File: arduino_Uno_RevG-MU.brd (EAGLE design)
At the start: 107 x 76.2 mm, 48 parts, among them IC3 ADC, U4 ARDUINOR3-DIMENSION

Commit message: updated
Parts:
- removed U$33: CS, LS_ELECTRIC:1X2_HEADER
- added U$14, U$15, U$16, U$17, U$20: 1X2_HEADER1X2, LS_ELECTRIC:1X2_HEADER
- moved U$9 10.1 mm to (86.0, 7.60), turned to 90 degrees
- moved R14 10.1 mm to (88.2, 7.68), turned to 270 degrees
- moved R5 7.53 mm to (88.2, 25.7), turned to 270 degrees
- moved U$3 7.52 mm to (86.0, 25.7), turned to 90 degrees
- moved R15 6.59 mm to (88.2, 66.2), turned to 90 degrees
- moved U$12 6.54 mm to (86.1, 66.2), turned to 90 degrees
- moved U$10 6.31 mm to (90.7, 9.62), turned to 90 degrees
- moved U$36 5.25 mm to (93.9, 65.6)
- moved U$6 4.46 mm to (86.1, 44.0), turned to 90 degrees
- moved R7 4.43 mm to (88.2, 44.0), turned to 270 degrees
- moved R6 3.91 mm to (88.1, 48.1), turned to 90 degrees
- moved U$4 3.86 mm to (86.1, 48.0), turned to 90 degrees
- moved U$34 3.76 mm to (93.9, 10.9)
- moved U$11 3.62 mm to (90.7, 27.6), turned to 90 degrees
- moved U$19 2.76 mm to (90.6, 64.3), turned to 90 degrees
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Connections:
- removed net IO6: U4.D6
- new net N$4: U$20.2, U$40.4
- new net N$5: U$20.1, U$40.5
- new net SS0: U$14.1, U4.D10
- new net SS1: U$15.1, U4.D8
- new net SS2: U$16.1, U4.D7
- new net SS3: U$17.1, U4.D6
- net CS3: no longer U$33.1
- net CS4: no longer U$33.2
- net IO4: now also U$40.2; no longer U$40.4
- net IO5: now also U$40.1; no longer U$40.5
- net N$11: now also U$1.GND_INV
- net N$15: now also U$36.GND_INV
- net N$23: now also U$34.GND_INV
- net N$34: now also U$35.GND_INV
- net RX: no longer U$40.1
- net SS: now also U$14.2, U$15.2, U$16.2, U$17.2; no longer U4.D10
- net TX: no longer U$40.2
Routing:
- net TX: track 60.7 -> 0.00 mm
- net RX: track 60.4 -> 0.00 mm
- net SS: track 12.0 -> 41.1 mm, vias 0 -> 2
- net IO5: track 65.9 -> 45.6 mm
- net 5VDC_COM_I: track 134.0 -> 149.2 mm, vias 12 -> 5
- net N$15: track 5.91 -> 16.3 mm
- net N$23: track 5.92 -> 16.2 mm
- net N$11: track 5.92 -> 16.2 mm
- net N$34: track 5.98 -> 16.0 mm
- net IO4: track 65.0 -> 55.5 mm, vias 1 -> 3
- net SS3: track 0.00 -> 8.86 mm
- net SS0: track 0.00 -> 8.11 mm
- net SS2: track 0.00 -> 8.05 mm
- net SS1: track 0.00 -> 7.99 mm
- net CS3: track 7.75 -> 0.00 mm
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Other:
- board text added: "DI_4"
- board text added: "DI_5"
- board text added: "INT1"

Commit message: First board order
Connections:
- net 24GND renamed P_GND
- net 24VDC renamed PWR
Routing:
- net PWR: track 7.48 -> 6.94 mm
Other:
- board text added: "5V+"
- board text added: "GND"
- board text added: "PROX"
- board text added: "PWR"
- board text added: "P_GND"
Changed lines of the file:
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@@
 <text x="13.6" y="55.6" size="1.27" layer="21">DI_4</text>
 <text x="13.4" y="58.4" size="1.27" layer="21">DI_5</text>
+<text x="13.6" y="15.5" size="1.016" layer="21">PWR</text>
+<text x="13" y="17.9" size="1.016" layer="21">PROX</text>
+<text x="12.9" y="26.5" size="1.016" layer="21">P_GND</text>
+<text x="12.7" y="31" size="1.016" layer="21">GND</text>
+<text x="12.8" y="36.2" size="1.016" layer="21">5V+</text>
 </plain>
 <attributes>
@@
 <wire x1="16.285" y1="22.4" x2="16.245" y2="22.44" width="0.254" layer="1"/>
 </signal>
-<signal name="24GND">
-<contactref element="OP1" pad="3_CAT"/>
-<contactref element="C22" pad="2"/>
-<wire x1="14.3" y1="26.1" x2="14.3" y2="24.63" width="0.254" layer="1"/>
-<wire x1="14.355" y1="24.575" x2="14.3" y2="24.63" width="0.254" layer="1"/>
-<wire x1="18.39" y1="23.86" x2="19.86" y2="23.86" width="0.254" layer="1"/>
-<wire x1="19.86" y1="23.86" x2="19.9" y2="23.9" width="0.254" layer="1"/>
-<via x="19.9" y="23.9" extent="1-16" drill="0.35"/>
-<wire x1="19.9" y1="23.9" x2="18.3" y2="23.9" width="0.254" layer="16"/>
-<wire x1="18.3" y1="23.9" x2="16.1" y2="26.1" width="0.254" layer="16"/>
-<wire x1="16.1" y1="26.1" x2="15.1" y2="26.1" width="0.254" layer="16"/>
-<via x="15.1" y="26.1" extent="1-16" drill="0.35"/>
-<wire x1="15.1" y1="26.1" x2="14.3" y2="26.1" width="0.254" layer="1"/>
-<contactref element="U$40" pad="8"/>
-<wire x1="10.175" y1="25.18" x2="10.78" y2="24.575" width="0.254" layer="1"/>
-<wire x1="10.78" y1="24.575" x2="14.355" y2="24.575" width="0.254" layer="1"/>
-</signal>
-<signal name="24VDC">
-<contactref element="R13" pad="1"/>
-<contactref element="U$40" pad="10"/>
-<wire x1="10.175" y1="15.1" x2="11.1" y2="15.1" width="0.254" layer="1"/>
-<wire x1="11.1" y1="15.1" x2="13.5" y2="17.5" width="0.254" layer="1"/>
-<wire x1="13.5" y1="17.5" x2="13.5" y2="19.465" width="0.254" layer="1"/>
-<wire x1="13.5" y1="19.465" x2="14.345" y2="20.31" width="0.254" layer="1"/>
-</signal>
 <signal name="PROX">
 <contactref element="R16" pad="1"/>
@@
 <wire x1="13.79" y1="40.42" x2="10.175" y2="40.42" width="0.254" layer="1"/>
 </signal>
+<signal name="PWR">
+<contactref element="R13" pad="1"/>
+<contactref element="U$40" pad="10"/>
+<wire x1="10.175" y1="15.1" x2="14.345" y2="19.27" width="0.254" layer="1"/>
+<wire x1="14.345" y1="19.27" x2="14.345" y2="20.31" width="0.254" layer="1"/>
+</signal>
+<signal name="P_GND">
+<contactref element="OP1" pad="3_CAT"/>
+<contactref element="C22" pad="2"/>
+<wire x1="14.3" y1="26.1" x2="14.3" y2="24.63" width="0.254" layer="1"/>
+<wire x1="14.355" y1="24.575" x2="14.3" y2="24.63" width="0.254" layer="1"/>
+<wire x1="18.39" y1="23.86" x2="19.86" y2="23.86" width="0.254" layer="1"/>
+<wire x1="19.86" y1="23.86" x2="19.9" y2="23.9" width="0.254" layer="1"/>
+<via x="19.9" y="23.9" extent="1-16" drill="0.35"/>
+<wire x1="19.9" y1="23.9" x2="18.3" y2="23.9" width="0.254" layer="16"/>
+<wire x1="18.3" y1="23.9" x2="16.1" y2="26.1" width="0.254" layer="16"/>
+<wire x1="16.1" y1="26.1" x2="15.1" y2="26.1" width="0.254" layer="16"/>
+<via x="15.1" y="26.1" extent="1-16" drill="0.35"/>
+<wire x1="15.1" y1="26.1" x2="14.3" y2="26.1" width="0.254" layer="1"/>
+<contactref element="U$40" pad="8"/>
+<wire x1="10.175" y1="25.18" x2="12.02" y2="25.18" width="0.254" layer="1"/>
+<wire x1="12.02" y1="25.18" x2="12.6" y2="24.6" width="0.254" layer="1"/>
+<wire x1="12.6" y1="24.6" x2="14.33" y2="24.6" width="0.254" layer="1"/>
+<wire x1="14.33" y1="24.6" x2="14.355" y2="24.575" width="0.254" layer="1"/>
+</signal>
 </signals>

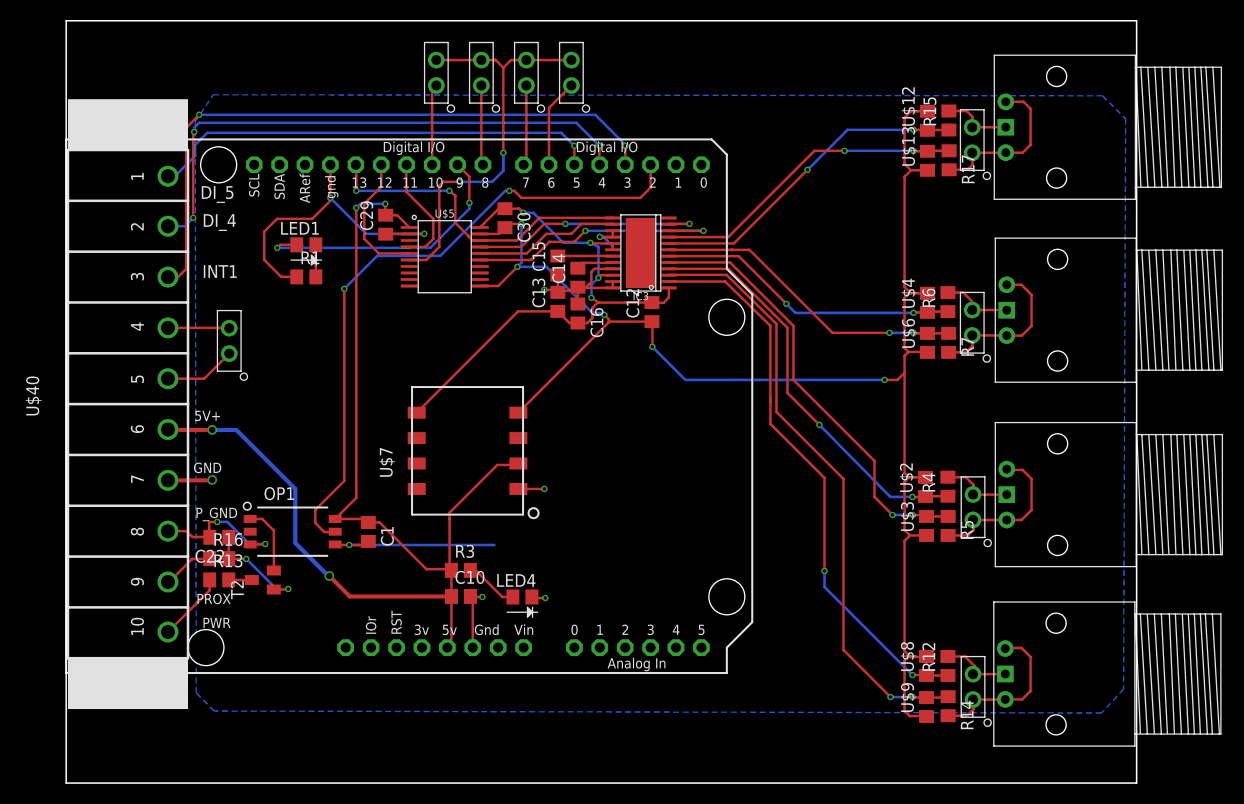
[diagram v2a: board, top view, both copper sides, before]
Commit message: changed to 99mm board
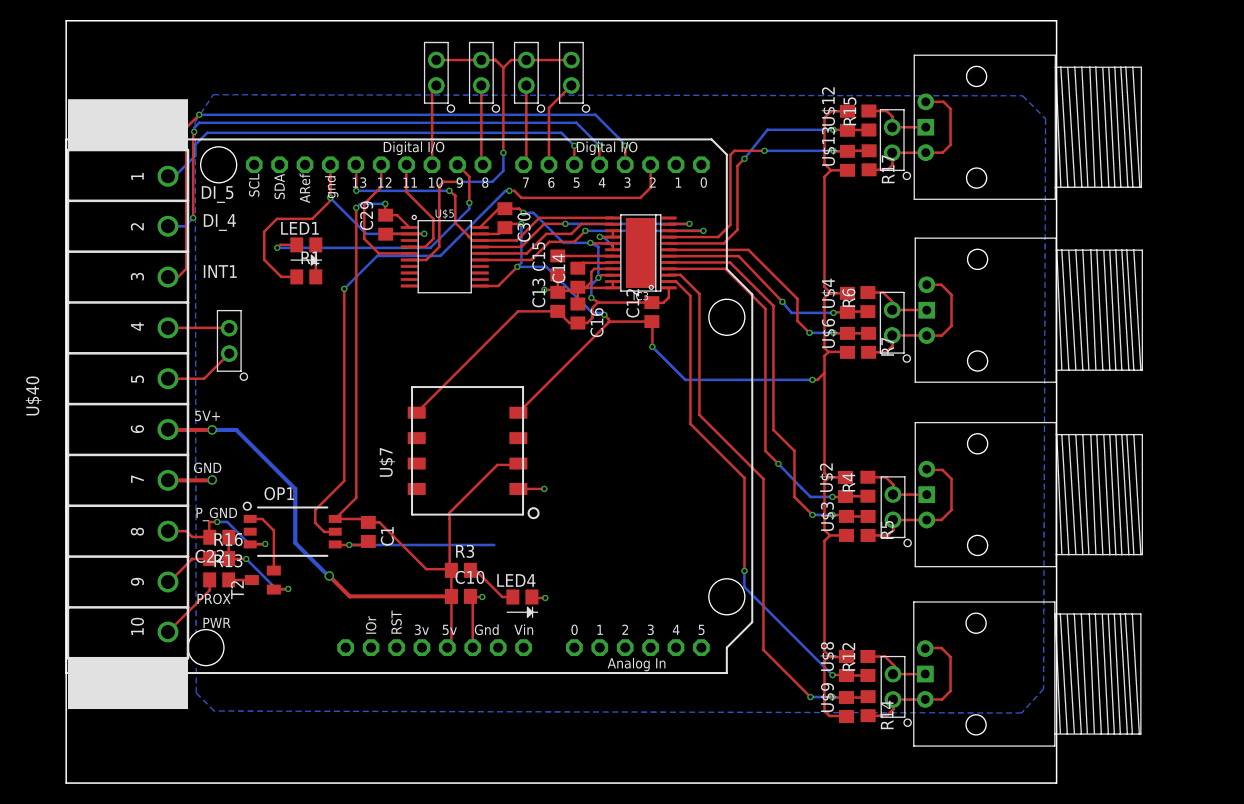
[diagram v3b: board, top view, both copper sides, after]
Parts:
- moved R12 8.00 mm to (80.1, 11.7)
- moved R14 8.00 mm to (80.2, 7.68)
- moved R15 8.00 mm to (80.2, 66.2)
- moved R17 8.00 mm to (80.3, 62.3)
- moved R4 8.00 mm to (80.1, 29.6)
- moved R5 8.00 mm to (80.2, 25.7)
- moved R6 8.00 mm to (80.1, 48.1)
- moved R7 8.00 mm to (80.2, 44.0)
- moved U$1 8.00 mm to (86.0, 28.8)
- moved U$10 8.00 mm to (82.7, 9.62)
- moved U$11 8.00 mm to (82.7, 27.6)
- moved U$12 8.00 mm to (78.1, 66.2)
- moved U$13 8.00 mm to (78.1, 62.2)
- moved U$18 8.00 mm to (82.6, 46.0)
- moved U$19 8.00 mm to (82.6, 64.3)
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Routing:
- net 5VDC_COM_I: track 149.2 -> 141.2 mm
- net CH2: track 30.3 -> 22.4 mm
- net CH2_COM: track 31.5 -> 24.7 mm
- net CH0: track 56.3 -> 50.1 mm
- net CH0_COM: track 60.6 -> 54.6 mm
- net CH3: track 32.7 -> 28.7 mm
- net CH3_COM: track 31.6 -> 27.7 mm
- net CH1: track 41.2 -> 37.7 mm
- net CH1_COM: track 43.7 -> 40.4 mm
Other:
- board size 107 x 76.2 mm -> 99 x 76.2 mm
